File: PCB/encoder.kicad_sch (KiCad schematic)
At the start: 42 parts, among them J8 ->ESP32, SW3 EC11E15244B2, SW6 Back, U23 TPS7B92033DBVR, U24 TCA9535PWR

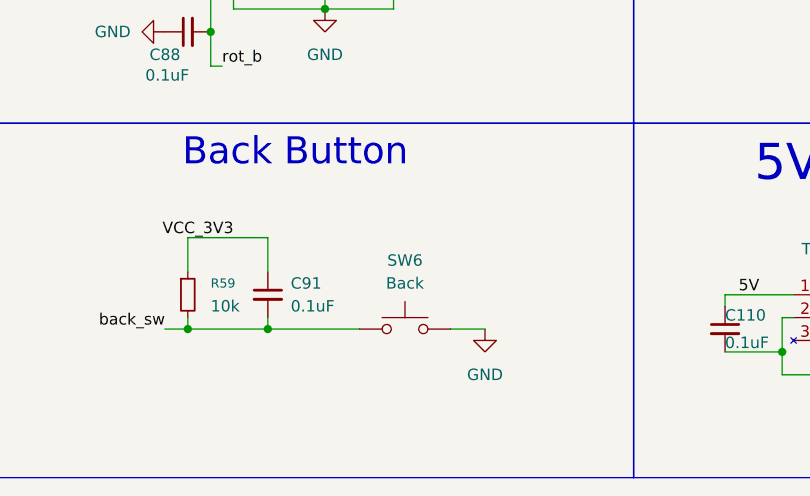
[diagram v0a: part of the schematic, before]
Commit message: updated button name and gitignore to (for now) block lvgl stuff
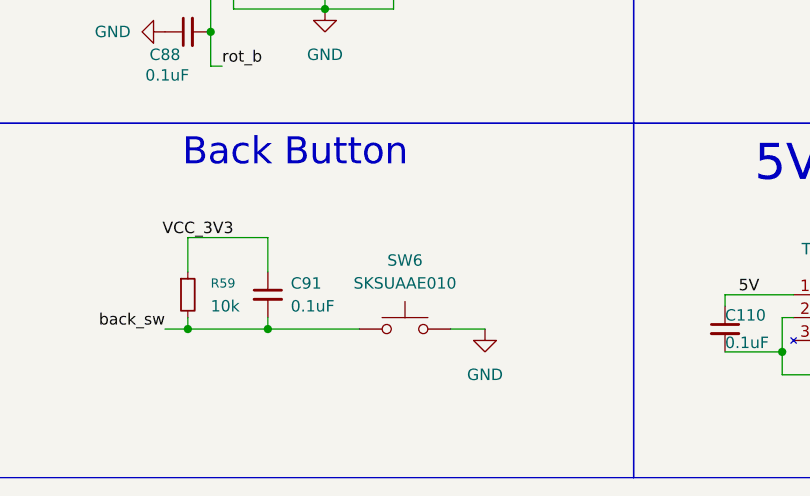
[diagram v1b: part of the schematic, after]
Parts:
- SW6: value Back -> SKSUAAE010
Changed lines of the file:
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@@
 			)
 		)
-		(property "Value" "Back"
+		(property "Value" "SKSUAAE010"
 			(at 152.4 129.54 0)
 			(effects

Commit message: Saving my work on PCB and other files
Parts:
- added J11: OPT, Connector_PinHeader_2.54mm:PinHeader_1x03_P2.54mm_Vertical, symbol Connector_Generic:Conn_01x03
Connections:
- net at U24.10 (P06): now also J11.3 (Pin_3)
- net at U24.8 (P04): now also J11.1 (Pin_1)
- net at U24.9 (P05): now also J11.2 (Pin_2)
- no-connect marks 13 -> 10
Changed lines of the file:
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@@
 	)
 	(junction
-		(at 194.31 137.16)
-		(diameter 0)
-		(color 0 0 0 0)
-	)
-	(junction
 		(at 54.61 115.57)
 		(diameter 0)
@@
 	)
 	(junction
+		(at 194.31 139.7)
+		(diameter 0)
+		(color 0 0 0 0)
+	)
+	(junction
 		(at 119.38 22.86)
 		(diameter 0)
@@
 	)
 	(no_connect
-		(at 90.17 87.63)
-	)
-	(no_connect
 		(at 90.17 115.57)
 	)
@@
 	)
 	(no_connect
-		(at 90.17 92.71)
-	)
-	(no_connect
 		(at 90.17 107.95)
 	)
 	(no_connect
-		(at 90.17 90.17)
-	)
-	(no_connect
 		(at 233.68 35.56)
 	)
@@
 	(wire
 		(pts
-			(xy 194.31 137.16) (xy 194.31 139.7)
+			(xy 201.93 22.86) (xy 210.82 22.86)
 		)
 		(stroke
@@
 	(wire
 		(pts
-			(xy 201.93 22.86) (xy 210.82 22.86)
+			(xy 143.51 99.06) (xy 133.35 99.06)
 		)
 		(stroke
@@
 	(wire
 		(pts
-			(xy 143.51 99.06) (xy 133.35 99.06)
+			(xy 194.31 139.7) (xy 187.96 139.7)
 		)
 		(stroke
@@
 	(wire
 		(pts
-			(xy 194.31 137.16) (xy 187.96 137.16)
+			(xy 187.96 139.7) (xy 187.96 137.16)
 		)
 		(stroke
@@
 	(wire
 		(pts
+			(xy 194.31 133.35) (xy 194.31 139.7)
+		)
+		(stroke
+			(width 0)
+			(type default)
+		)
+	)
+	(wire
+		(pts
 			(xy 128.27 124.46) (xy 128.27 128.27)
 		)
@@
 	(wire
 		(pts
-			(xy 194.31 133.35) (xy 194.31 137.16)
-		)
-		(stroke
-			(width 0)
-			(type default)
-		)
-	)
-	(wire
-		(pts
 			(xy 48.26 22.86) (xy 48.26 40.64)
 		)
@@
 	)
 	(symbol
+		(lib_id "Connector_Generic:Conn_01x03")
+		(at 95.25 90.17 0)
+		(unit 1)
+		(exclude_from_sim no)
+		(in_bom yes)
+		(on_board yes)
+		(dnp no)
+		(fields_autoplaced yes)
+		(property "Reference" "J11"
+			(at 97.79 88.8999 0)
+			(effects
+				(font
+					(size 1.27 1.27)
+				)
+				(justify left)
+			)
+		)
+		(property "Value" "OPT"
+			(at 97.79 91.4399 0)
+			(effects
+				(font
+					(size 1.27 1.27)
+				)
+				(justify left)
+			)
+		)
+		(property "Footprint" "Connector_PinHeader_2.54mm:PinHeader_1x03_P2.54mm_Vertical"
+			(at 95.25 90.17 0)
+			(effects
+				(font
+					(size 1.27 1.27)
+				)
+				(hide yes)
+			)
+		)
+		(property "Datasheet" "~"
+			(at 95.25 90.17 0)
+			(effects
+				(font
+					(size 1.27 1.27)
+				)
+				(hide yes)
+			)
+		)
+		(property "Description" "Generic connector, single row, 01x03, script generated (kicad-library-utils/schlib/autogen/connector/)"
+			(at 95.25 90.17 0)
+			(effects
+				(font
+					(size 1.27 1.27)
+				)
+				(hide yes)
+			)
+		)
+		(pin "2"
+		)
+		(pin "3"
+		)
+		(pin "1"
+		)
+		(instances
+			(project ""
+				(path "/08b9944e-0e9a-4685-98da-9a654683b13c/245bb5b0-daf4-45b9-ad72-e6163f4a1a2a/21b245af-c3d8-4405-bdbd-4fdd89fa37ec"
+					(reference "J11")
+					(unit 1)
+				)
+			)
+		)
+	)
+	(symbol
 		(lib_id "Switch:SW_Push")
 		(at 152.4 134.62 0)
@@
 		)
 		(property "Value" "0.1uF"
-			(at 187.96 136.144 0)
+			(at 187.96 136.398 0)
 			(effects
 				(font
